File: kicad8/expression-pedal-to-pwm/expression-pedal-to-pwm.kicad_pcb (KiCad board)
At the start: 2 copper layers, 67 x 61.5 mm, 36 parts, among them J4 NMJ6HHD2, J5 Screw_Terminal_01x06, Q1 STP100N8F6, SW1 SW_Push_DPDT, U1 TLV2374, U2 LM7805_TO220

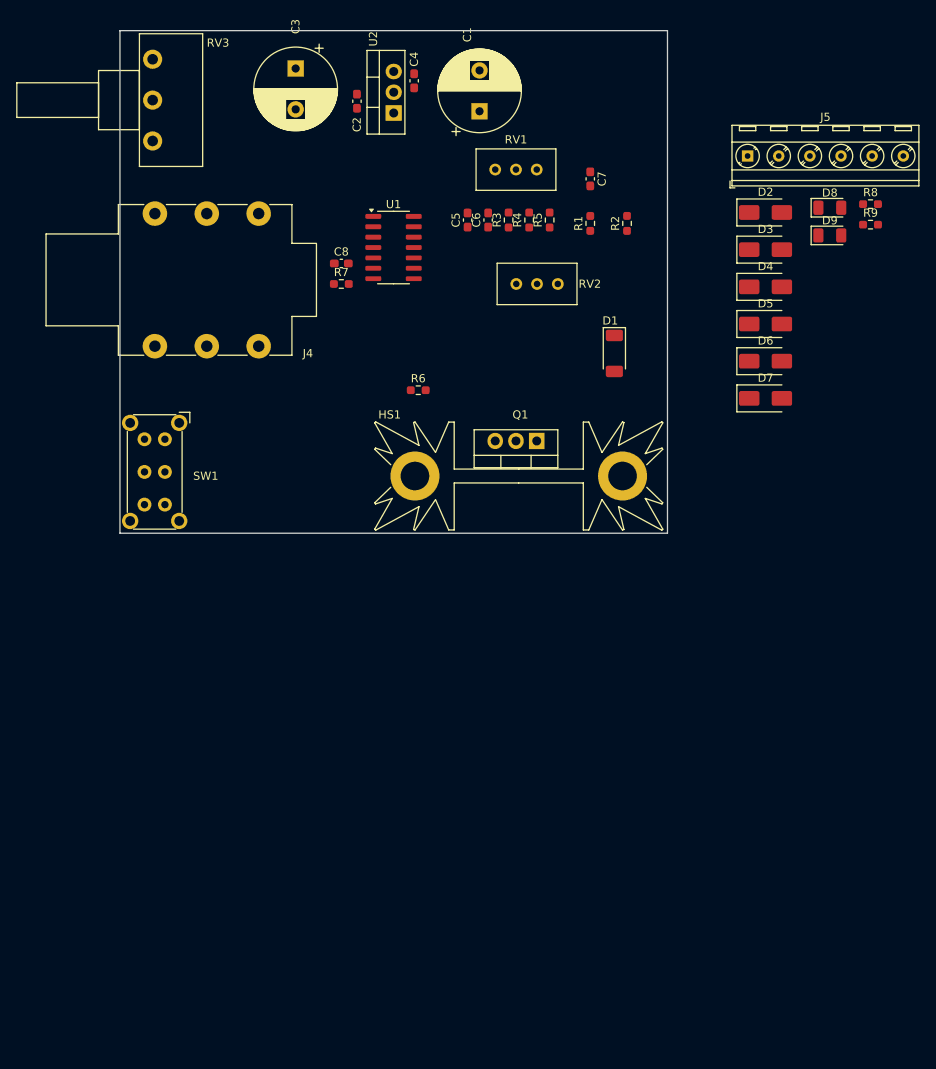
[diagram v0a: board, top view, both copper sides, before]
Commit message: Layout components and traces for Expression Pedal PWM Motor Controller
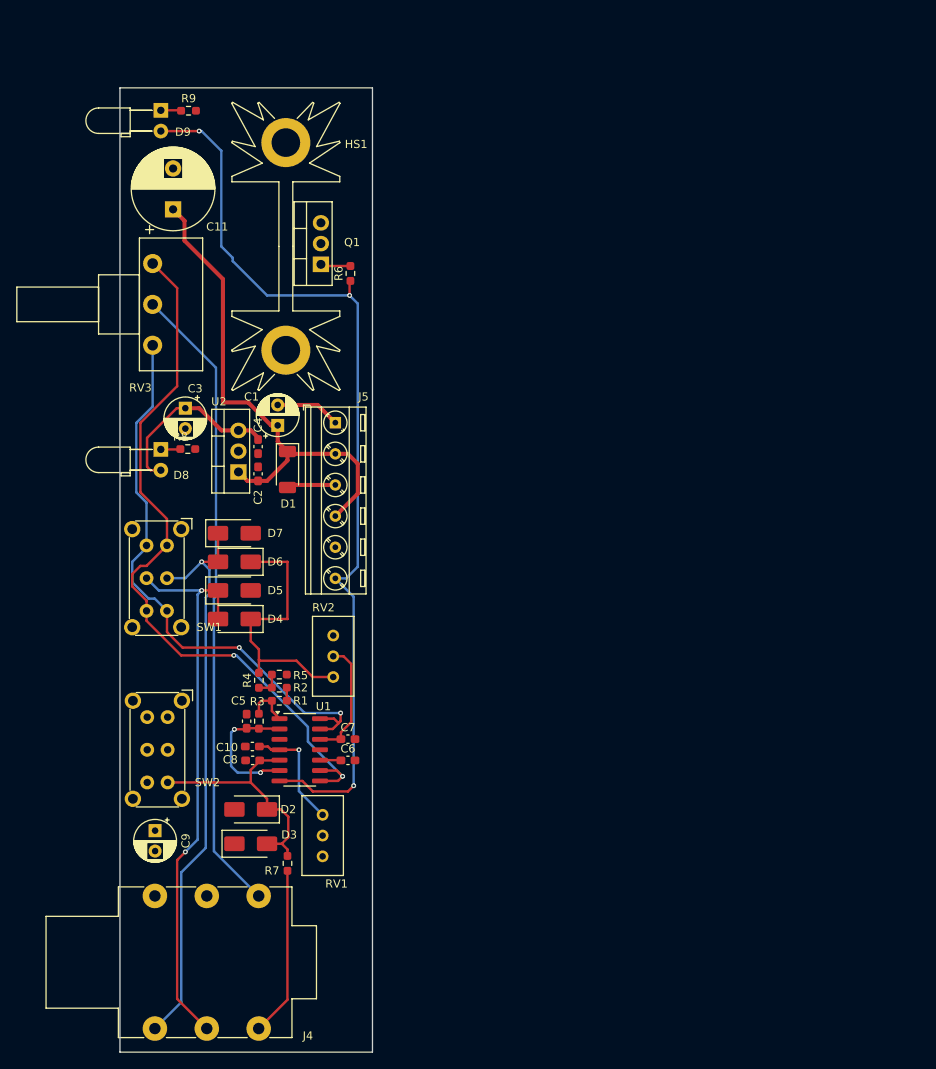
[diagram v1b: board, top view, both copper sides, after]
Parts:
- added C10: 100n, Capacitor_SMD:C_0603_1608Metric_Pad1.08x0.95mm_HandSolder, F.Cu at (125.2, 155.1)
- added C11: 1000u, Capacitor_THT:CP_Radial_D10.0mm_P5.00mm, F.Cu at (115.5, 89.4)
- added C9: 10u, Capacitor_THT:CP_Radial_D5.0mm_P2.50mm, F.Cu at (113.3, 165.4)
- added SW2: SW_Push_DPDT, Button_Switch_THT:SW_E-Switch_EG2219_DPDT_Angled, F.Cu at (114.8, 151.5)
- C1, C3: footprint Capacitor_THT:CP_Radial_D10.0mm_P5.00mm -> Capacitor_THT:CP_Radial_D5.0mm_P2.50mm
- C8: value 100n -> 47n
- D8, D9: footprint LED_SMD:LED_1206_3216Metric -> LED_THT:LED_D3.0mm_Horizontal_O3.81mm_Z6.0mm
- R7: value 1K -> 1M
- moved D2 96.5 mm to (125.0, 162.8), turned to 180 degrees
- moved D3 96.2 mm to (125.0, 167.0)
- moved R8 88.8 mm to (117.3, 118.7), turned to 180 degrees
- moved D8 87.0 mm to (114.0, 118.8), turned to -90 degrees
- moved R9 84.6 mm to (117.4, 77.3), turned to 180 degrees
- moved J4 83.5 mm to (126.0, 189.6)
- moved D9 83.3 mm to (114.0, 77.2), turned to -90 degrees
- moved RV1 83.2 mm to (133.8, 163.5), turned to 90 degrees
- moved D4 76.7 mm to (123.0, 139.5), turned to 180 degrees
- moved C7 74.7 mm to (136.9, 154.2), turned to 0 degrees
- moved D5 72.7 mm to (123.0, 136.0)
- moved R7 71.2 mm to (129.5, 169.4), turned to -90 degrees
- moved R2 71.0 mm to (128.5, 147.9), turned to 0 degrees
- moved R1 69.7 mm to (128.5, 149.5), turned to 180 degrees
- moved D6 69.5 mm to (123.0, 132.5), turned to 180 degrees
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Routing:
- net /PWM: track 0.00 -> 113.5 mm, vias 0 -> 3
- net VREF_LOW: track 0.00 -> 90.1 mm, vias 0 -> 2
- net Net-(J4-PadTN): track 0.00 -> 78.0 mm
- net VREF_HIGH: track 0.00 -> 71.1 mm, vias 0 -> 2
- net /Sleeve: track 0.00 -> 70.9 mm, vias 0 -> 1
- net 5V: track 0.00 -> 69.4 mm, vias 0 -> 1
- net /Ring: track 0.00 -> 69.2 mm, vias 0 -> 2
- net /Power In: track 0.00 -> 63.1 mm
- net /Tip_filtered: track 0.00 -> 30.1 mm
- net /Tip: track 0.00 -> 20.8 mm
- net /OscillatorVoltage: track 0.00 -> 16.7 mm, vias 0 -> 2
- net Net-(U1D-+): track 0.00 -> 14.9 mm
- net GND: track 0.00 -> 7.95 mm
- net Net-(D1-A): track 0.00 -> 5.98 mm
- net Net-(R1-Pad2): track 0.00 -> 5.58 mm
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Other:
- board size 67 x 61.5 mm -> 30.9 x 118 mm

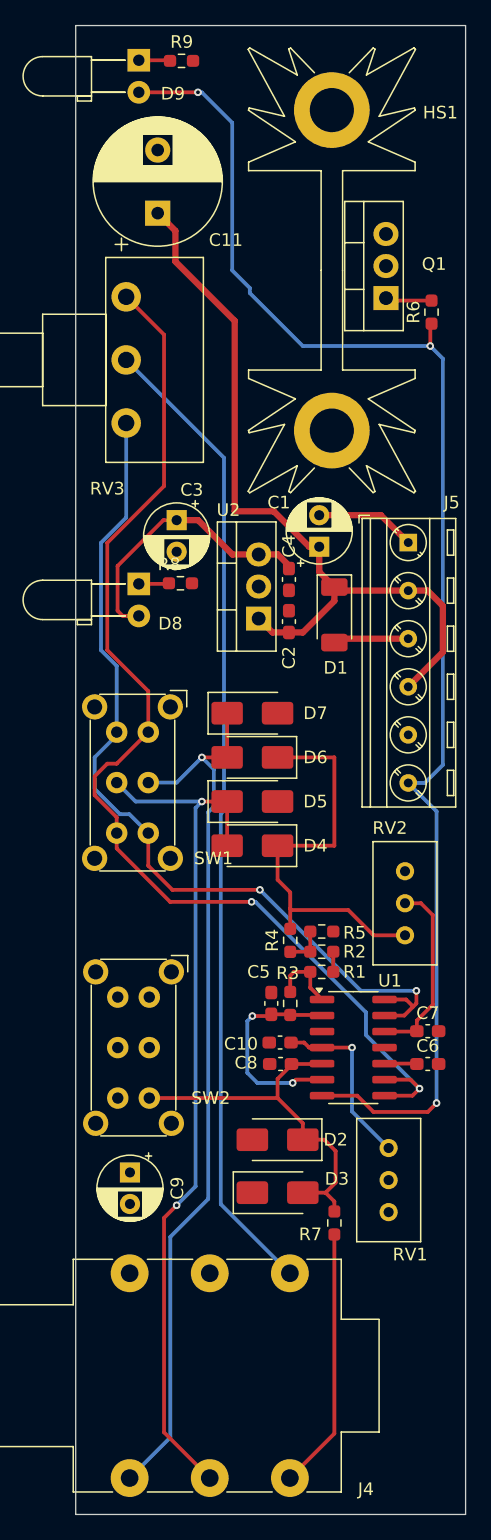
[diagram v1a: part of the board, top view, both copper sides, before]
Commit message: Add copper pour and via stitching to Expression-Pedal-to-PWM
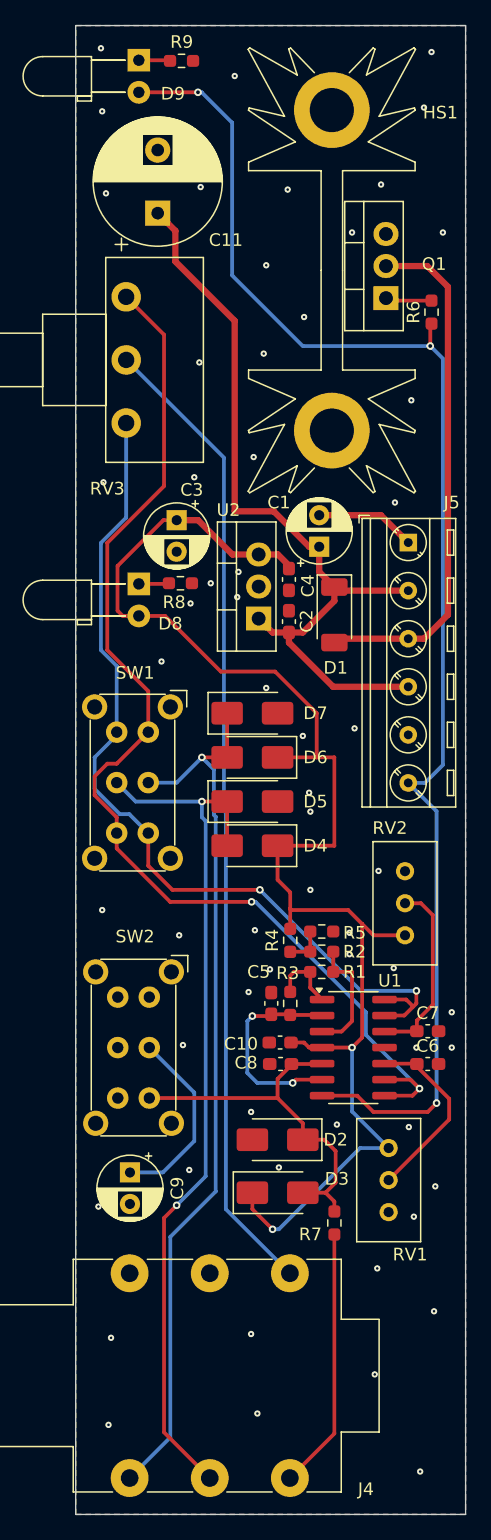
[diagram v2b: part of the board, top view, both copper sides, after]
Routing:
- net 5V: track 69.4 -> 115.7 mm, vias 1 -> 2
- net Net-(D1-A): track 5.98 -> 41.5 mm
- net Net-(C9-Pad1): track 0.00 -> 15.0 mm
- net Net-(U1C-+): track 2.57 -> 14.8 mm
- net Net-(U1A-+): track 1.60 -> 9.71 mm
- net /Power In: track 63.1 -> 64.0 mm
- net GND: vias 0 -> 60
- added copper zone on B.Cu, net GND
- added copper zone on F.Cu, net GND

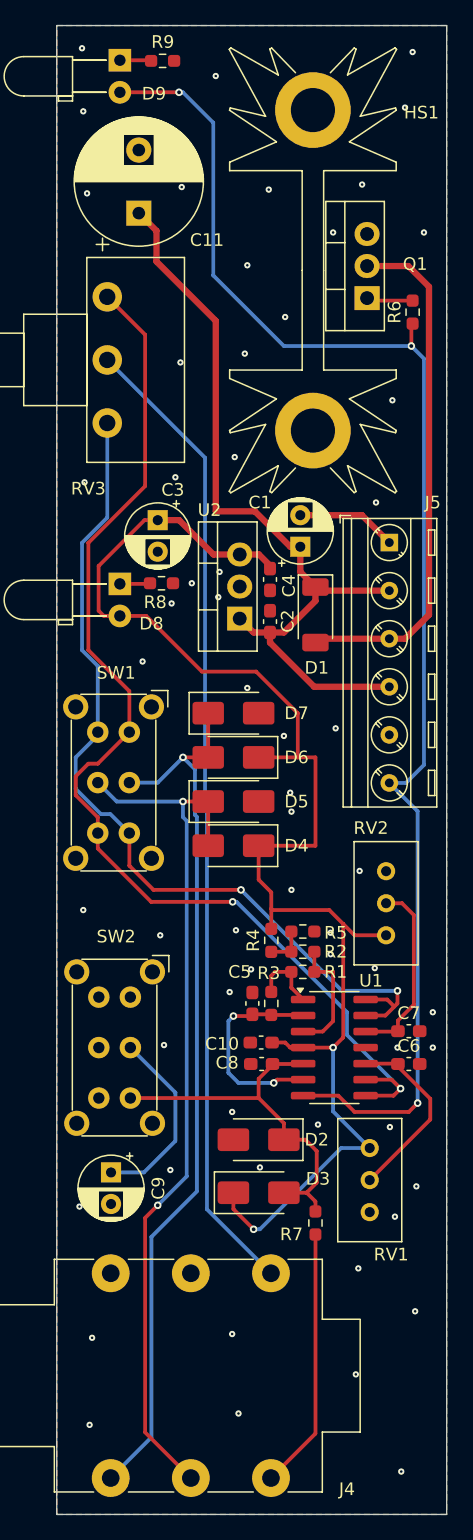
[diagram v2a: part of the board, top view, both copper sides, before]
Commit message: Export Rev 1 Expression Pedal to PWM
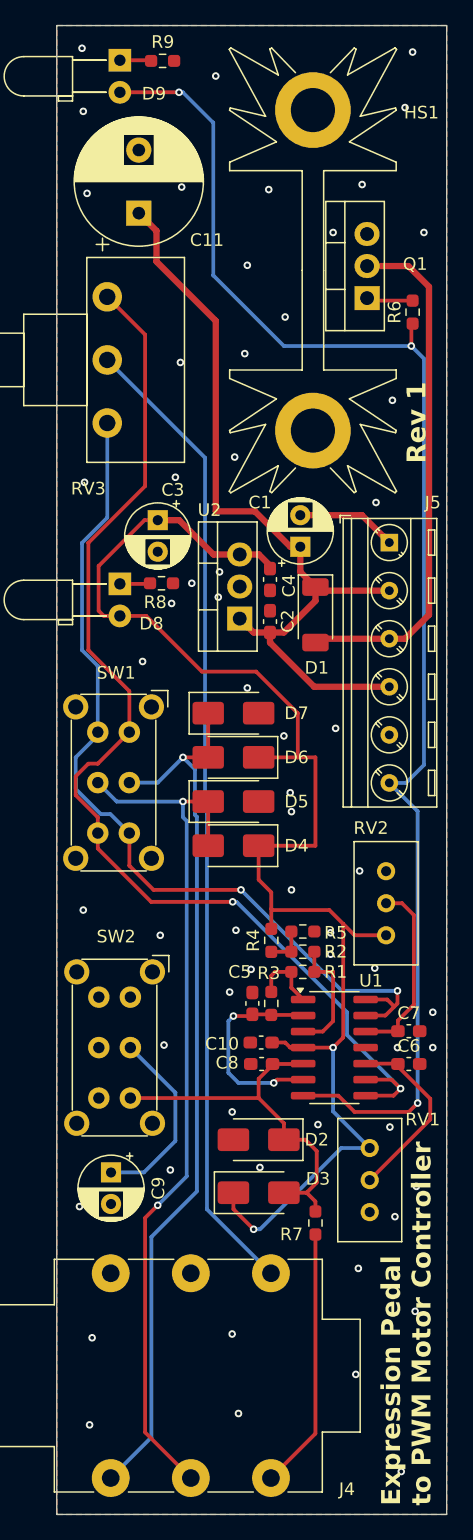
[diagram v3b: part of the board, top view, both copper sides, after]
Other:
- board text added: "Expression Pedal to PWM Motor Controller"
- board text added: "Rev 1"

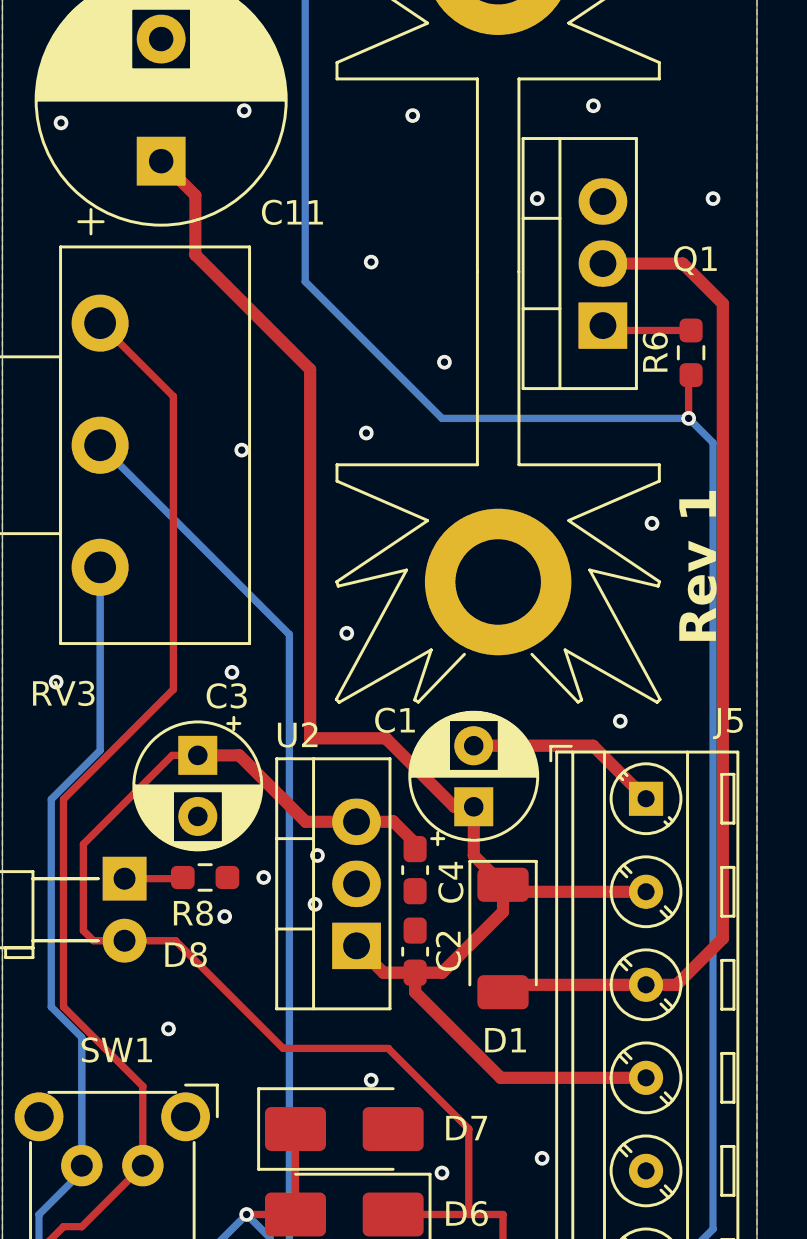
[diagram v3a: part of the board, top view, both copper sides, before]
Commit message: Increased the size of the motor traces
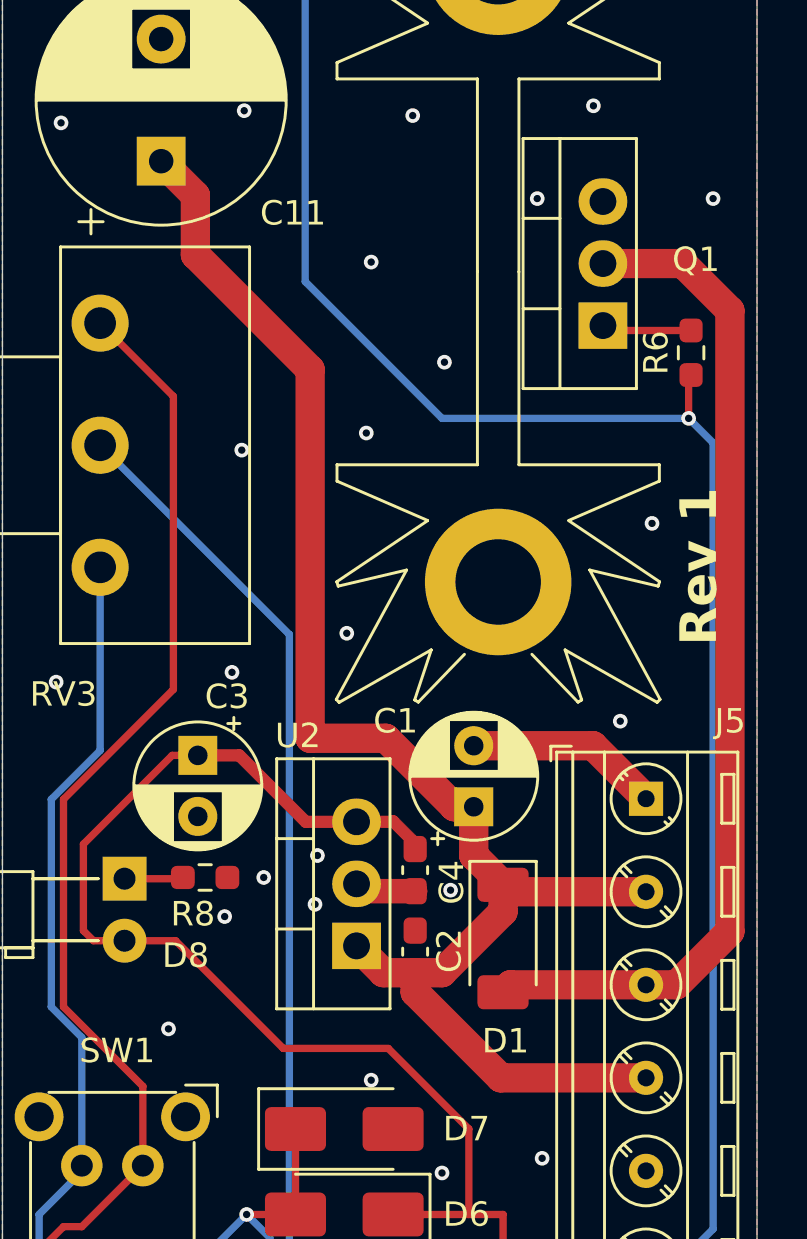
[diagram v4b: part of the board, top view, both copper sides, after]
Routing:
- net GND: track 7.95 -> 10.5 mm, vias 60 -> 61
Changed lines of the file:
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@@
 		(start 135.355 115.475)
 		(end 133.185113 113.305113)
-		(width 0.5)
+		(width 1.2)
 		(layer "F.Cu")
 		(net 8)
@@
 		(start 133.185113 113.305113)
 		(end 128.3 113.305113)
-		(width 0.5)
+		(width 1.2)
+		(layer "F.Cu")
+		(net 8)
+	)
+	(segment
+		(start 123.5 118.96)
+		(end 123.8 119.26)
+		(width 1)
+		(layer "F.Cu")
+		(net 8)
+	)
+	(segment
+		(start 125.8975 119.26)
+		(end 125.9 119.2625)
+		(width 1)
+		(layer "F.Cu")
+		(net 8)
+	)
+	(segment
+		(start 123.8 119.26)
+		(end 125.8975 119.26)
+		(width 1)
 		(layer "F.Cu")
 		(net 8)
@@
 	(via
 		(at 132.9 173)
+		(size 0.6)
+		(drill 0.3)
+		(layers "F.Cu" "B.Cu")
+		(free yes)
+		(net 8)
+	)
+	(via
+		(at 127.35 119.22)
 		(size 0.6)
 		(drill 0.3)
@@
 		(start 127 122.6)
 		(end 129.5 120.1)
-		(width 0.5)
+		(width 1.2)
 		(layer "F.Cu")
 		(net 15)
@@
 		(start 129.405 126.905)
 		(end 125.9 123.4)
-		(width 0.5)
+		(width 1.2)
 		(layer "F.Cu")
 		(net 15)
@@
 		(start 135.355 126.905)
 		(end 129.405 126.905)
-		(width 0.5)
+		(width 1.2)
 		(layer "F.Cu")
 		(net 15)
@@
 		(start 123.5 121.5)
 		(end 124.6 122.6)
-		(width 0.5)
+		(width 1.2)
 		(layer "F.Cu")
 		(net 15)
@@
 		(start 124.6 122.6)
 		(end 125.9 122.6)
-		(width 0.5)
+		(width 1.2)
 		(layer "F.Cu")
 		(net 15)
@@
 		(start 116.9 93.2)
 		(end 121.6 97.9)
-		(width 0.5)
+		(width 1.2)
 		(layer "F.Cu")
 		(net 15)
@@
 		(start 128.3 115.805113)
 		(end 128.3 117.8)
-		(width 0.5)
+		(width 1.2)
 		(layer "F.Cu")
 		(net 15)
@@
 		(start 127.505113 115.805113)
 		(end 128.3 115.805113)
-		(width 0.5)
+		(width 1.2)
 		(layer "F.Cu")
 		(net 15)
@@
 		(start 115.5 89.367677)
 		(end 116.9 90.767677)
-		(width 0.5)
+		(width 1.2)
 		(layer "F.Cu")
 		(net 15)
@@
 		(start 129.5 120.1)
 		(end 129.5 119)
-		(width 0.5)
+		(width 1.2)
 		(layer "F.Cu")
 		(net 15)
@@
 		(start 124.7 113)
 		(end 127.505113 115.805113)
-		(width 0.5)
+		(width 1.2)
 		(layer "F.Cu")
 		(net 15)
@@
 		(start 125.9 122.6)
 		(end 127 122.6)
-		(width 0.5)
+		(width 1.2)
 		(layer "F.Cu")
 		(net 15)
@@
 		(start 128.3 117.8)
 		(end 129.5 119)
-		(width 0.5)
+		(width 1.2)
 		(layer "F.Cu")
 		(net 15)
@@
 		(start 116.9 90.767677)
 		(end 116.9 93.2)
-		(width 0.5)
+		(width 1.2)
 		(layer "F.Cu")
 		(net 15)
@@
 		(start 121.6 97.9)
 		(end 121.6 113)
-		(width 0.5)
+		(width 1.2)
 		(layer "F.Cu")
 		(net 15)
@@
 		(start 129.785 119.285)
 		(end 129.5 119)
-		(width 0.5)
+		(width 1.2)
 		(layer "F.Cu")
 		(net 15)
@@
 		(start 121.6 113)
 		(end 124.7 113)
-		(width 0.5)
+		(width 1.2)
 		(layer "F.Cu")
 		(net 15)
@@
 		(start 135.355 119.285)
 		(end 129.785 119.285)
-		(width 0.5)
+		(width 1.2)
 		(layer "F.Cu")
 		(net 15)
@@
 		(start 125.9 123.4)
 		(end 125.9 122.6)
-		(width 0.5)
+		(width 1.2)
 		(layer "F.Cu")
 		(net 15)
@@
 	)
 	(segment
-		(start 138.5 121.2)
-		(end 136.605 123.095)
-		(width 0.5)
-		(layer "F.Cu")
-		(net 19)
-	)
-	(segment
-		(start 136.86 93.56)
-		(end 138.5 95.2)
-		(width 0.5)
+		(start 138.79 95.49)
+		(end 138.79 120.91)
+		(width 1.2)
 		(layer "F.Cu")
 		(net 19)
@@
 		(start 129.805 123.095)
 		(end 129.5 123.4)
-		(width 0.5)
+		(width 1.2)
+		(layer "F.Cu")
+		(net 19)
+	)
+	(segment
+		(start 133.59 93.56)
+		(end 136.86 93.56)
+		(width 1.2)
+		(layer "F.Cu")
+		(net 19)
+	)
+	(segment
+		(start 136.605 123.095)
+		(end 135.355 123.095)
+		(width 1.2)
 		(layer "F.Cu")
 		(net 19)
@@
 		(start 135.355 123.095)
 		(end 129.805 123.095)
-		(width 0.5)
+		(width 1.2)
 		(layer "F.Cu")
 		(net 19)
 	)
 	(segment
-		(start 133.59 93.56)
-		(end 136.86 93.56)
-		(width 0.5)
+		(start 138.79 120.91)
+		(end 136.605 123.095)
+		(width 1.2)
 		(layer "F.Cu")
 		(net 19)
 	)
 	(segment
-		(start 136.605 123.095)
-		(end 135.355 123.095)
-		(width 0.5)
+		(start 136.86 93.56)
+		(end 138.79 95.49)
+		(width 1.2)
 		(layer "F.Cu")
 		(net 19)
-	)
-	(segment
-		(start 138.5 95.2)
-		(end 138.5 121.2)
-		(width 0.5)
-		(layer "F.Cu")
-		(net 19)
